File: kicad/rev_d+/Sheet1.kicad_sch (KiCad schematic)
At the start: 135 parts, among them J1 JUMPER, J11 JUMPER, J4 JUMPER, J7 JUMPER, Q1 14Mhz, X1 FDD34M, X2 IDE40M, X24 to extender/riser

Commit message: pentevo: rev D+: zx kbd
git-svn-id: svn://localhost/local-pentevo@1307 c6c76956-fad2-4150-a3a9-ea0a427205ba
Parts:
- removed R19: 390, R-CHIP, symbol eva-altium-import:Sheet1_0_RESCHIP
- removed VD3: LED, LED100, symbol eva-altium-import:Sheet1_0_mirrored_LED
- added VT10, VT9: BC857, Package_TO_SOT_SMD:SOT-23_Handsoldering, symbol Transistor_BJT:BC857
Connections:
- net GND: now also VT10.3 (C), VT9.3 (C)
- net ~{SDCS}: now also VT10.1 (B)
- net ILED: no longer names the net of X2.39 (~{DASP})
- net ILED: now also VT9.1 (B)
- new net ~{DISK_LED}: VT10.2 (E), VT9.2 (E)

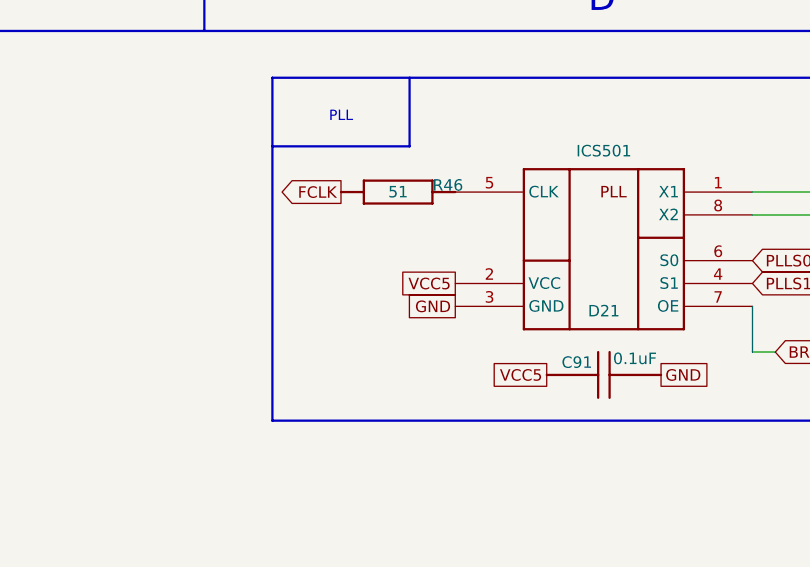
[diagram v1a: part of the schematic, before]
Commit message: pentevo: rev D+: return back shared UART between TTL and RS232, connect ROM high addrs to MCU
git-svn-id: svn://localhost/local-pentevo@1309 c6c76956-fad2-4150-a3a9-ea0a427205ba
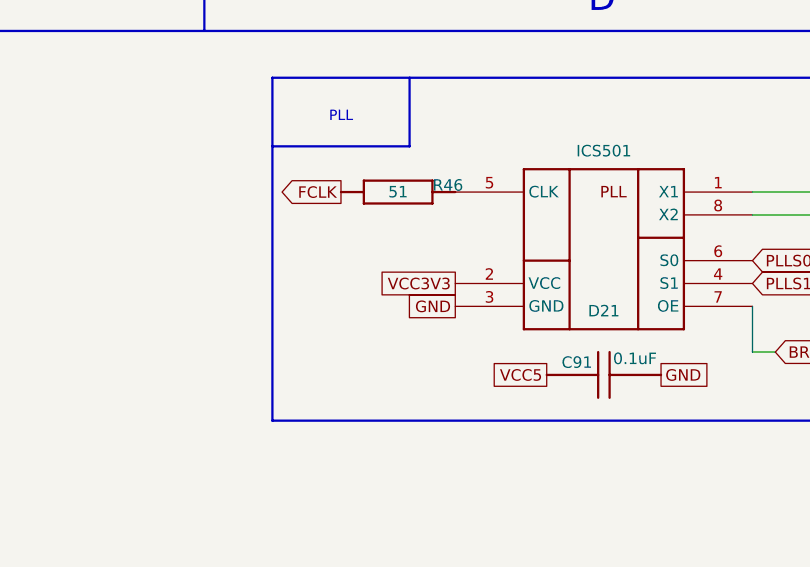
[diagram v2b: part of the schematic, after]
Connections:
- net VCC3V3: now also D21.2 (VCC)
- net VCC5: no longer D21.2 (VCC)
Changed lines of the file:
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@@
+		)
+	)
+	(global_label "VCC3V3"
+		(shape passive)
+		(at 307.34 55.88 180)
+		(fields_autoplaced yes)
+		(effects
+			(font
+				(size 1.27 1.27)
+			)
+			(justify right)
+		)
+		(property "Intersheetrefs" "${INTERSHEET_REFS}"
+			(at 298.3299 55.88 0)
+			(effects
+				(font
+					(size 1.27 1.27)
+				)
+				(justify right)
+				(hide yes)
+			)
 		)
 	)
@@
 			(effects
 				(font
-					(size 1.27 1.27)
-				)
-				(justify right)
-				(hide yes)
-			)
-		)
-	)
-	(global_label "VCC5"
-		(shape passive)
-		(at 307.34 55.88 180)
-		(fields_autoplaced yes)
-		(effects
-			(font
-				(size 1.27 1.27)
-			)
-			(justify right)
-		)
-		(property "Intersheetrefs" "${INTERSHEET_REFS}"
-			(at 300.628 55.88 0)
-			(effects
-				(font

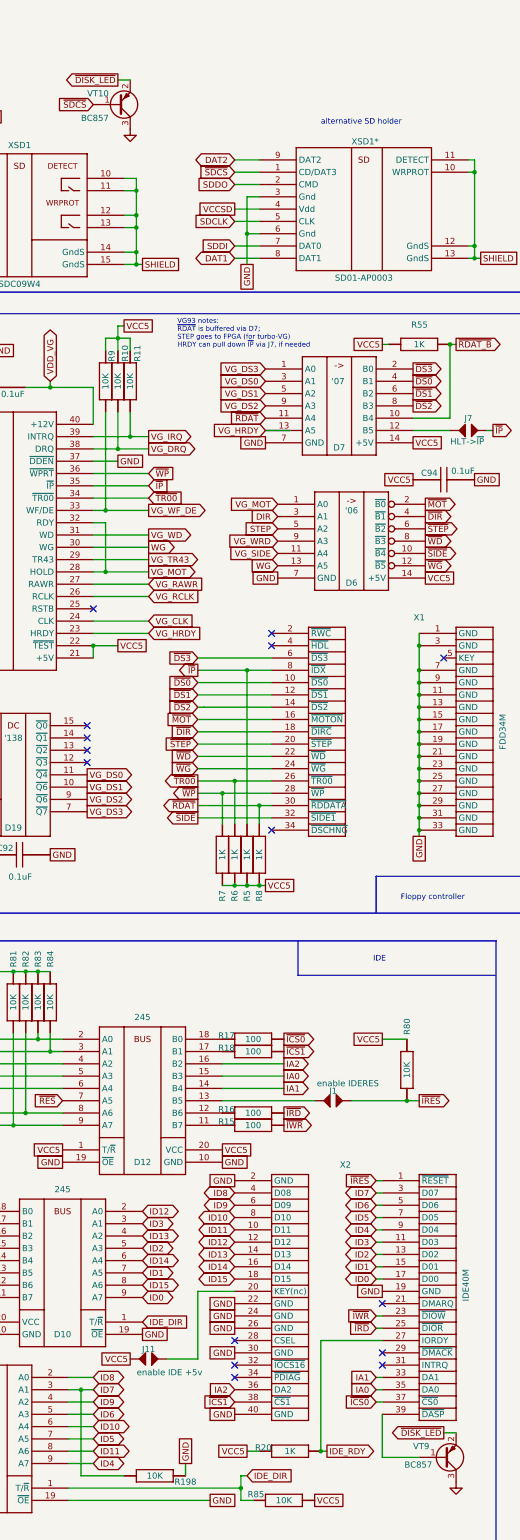
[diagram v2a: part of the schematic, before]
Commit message: pentevo: rev D+: fix I2C extender for segapads, remove 2N7002 from high ROM addresses, add I2C level convertor on 2N7002 (because of PCA9555 input levels)
git-svn-id: svn://localhost/local-pentevo@1311 c6c76956-fad2-4150-a3a9-ea0a427205ba
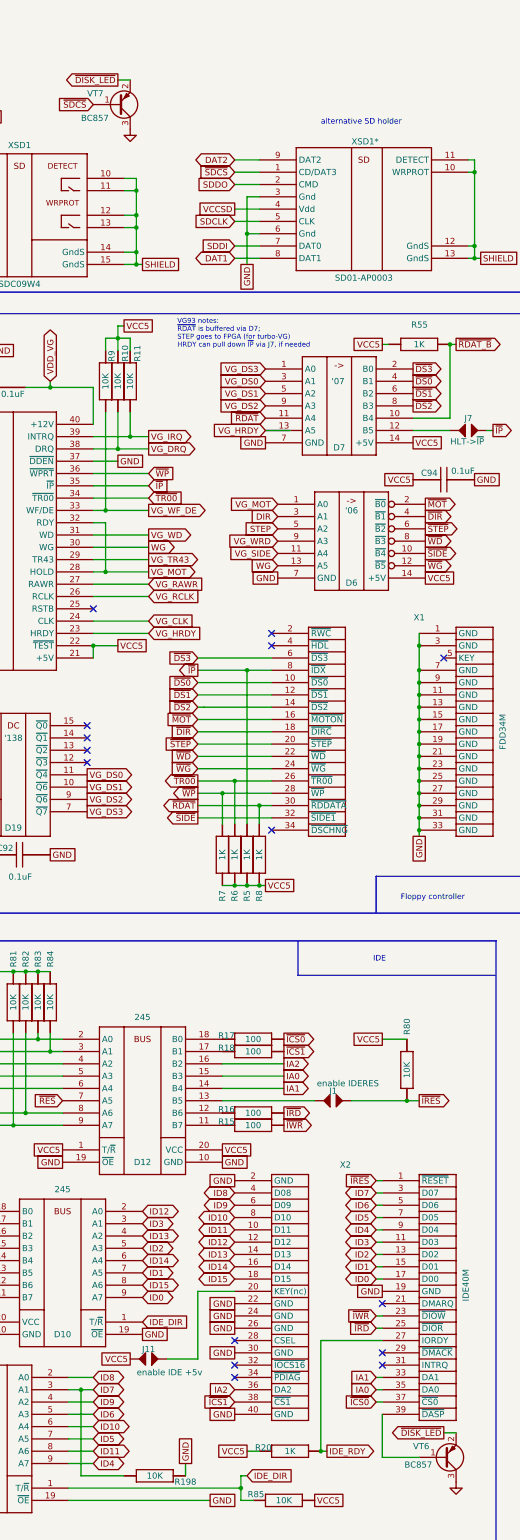
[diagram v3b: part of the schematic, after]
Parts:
- removed VT10, VT9: BC857, Package_TO_SOT_SMD:SOT-23_Handsoldering, symbol Transistor_BJT:BC857
- added VT6, VT7: BC857, Package_TO_SOT_SMD:SOT-23_Handsoldering, symbol Transistor_BJT:BC857
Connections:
- net GND: now also VT6.3 (C), VT7.3 (C)
- net ~{DISK_LED}: now also VT6.2 (E), VT7.2 (E)
- net ~{SDCS}: now also VT7.1 (B)
- net at X2.39 (~{DASP}): now also VT6.1 (B)
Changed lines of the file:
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@@
 	)
 	(symbol
-		(lib_id "Transistor_BJT:BC857")
-		(at 518.16 332.74 0)
-		(mirror x)
-		(unit 1)
-		(exclude_from_sim no)
-		(in_bom yes)
-		(on_board yes)
-		(dnp no)
-		(property "Reference" "VT9"
-			(at 511.81 330.454 0)
-			(effects
-				(font
-					(size 1.27 1.27)
-				)
-				(justify left)
-			)
-		)
-		(property "Value" "BC857"
-			(at 510.032 334.264 0)
-			(effects
-				(font
-					(size 1.27 1.27)
-				)
-				(justify left)
-			)
-		)
-		(property "Footprint" "Package_TO_SOT_SMD:SOT-23_Handsoldering"
-			(at 523.24 330.835 0)
-			(effects
-				(font
-					(size 1.27 1.27)
-					(italic yes)
-				)
-				(justify left)
-				(hide yes)
-			)
-		)
-		(property "Datasheet" "https://www.onsemi.com/pub/Collateral/BC860-D.pdf"
-			(at 518.16 332.74 0)
-			(effects
-				(font
-					(size 1.27 1.27)
-				)
-				(justify left)
-				(hide yes)
-			)
-		)
-		(property "Description" "0.1A Ic, 45V Vce, PNP Transistor, SOT-23"
-			(at 518.16 332.74 0)
-			(effects
-				(font
-					(size 1.27 1.27)
-				)
-				(hide yes)
-			)
-		)
-		(pin "1"
-		)
-		(pin "2"
-		)
-		(pin "3"
-		)
-		(instances
-			(project "eva"
-				(path "/ab605654-a730-497b-9e09-9b351f74b935/df95af23-acf0-4751-87c3-fbc71e0508c6"
-					(reference "VT9")
-					(unit 1)
-				)
-			)
-		)
-	)
-	(symbol
 		(lib_id "eva-altium-import:Sheet1_0_mirrored_04")
 		(at 147.32 59.69 0)
@@
 	)
 	(symbol
+		(lib_id "Transistor_BJT:BC857")
+		(at 450.85 53.34 0)
+		(mirror x)
+		(unit 1)
+		(exclude_from_sim no)
+		(in_bom yes)
+		(on_board yes)
+		(dnp no)
+		(property "Reference" "VT7"
+			(at 444.5 51.054 0)
+			(effects
+				(font
+					(size 1.27 1.27)
+				)
+				(justify left)
+			)
+		)
+		(property "Value" "BC857"
+			(at 443.23 56.134 0)
+			(effects
+				(font
+					(size 1.27 1.27)
+				)
+				(justify left)
+			)
+		)
+		(property "Footprint" "Package_TO_SOT_SMD:SOT-23_Handsoldering"
+			(at 455.93 51.435 0)
+			(effects
+				(font
+					(size 1.27 1.27)
+					(italic yes)
+				)
+				(justify left)
+				(hide yes)
+			)
+		)
+		(property "Datasheet" "https://www.onsemi.com/pub/Collateral/BC860-D.pdf"
+			(at 450.85 53.34 0)
+			(effects
+				(font
+					(size 1.27 1.27)
+				)
+				(justify left)
+				(hide yes)
+			)
+		)
+		(property "Description" "0.1A Ic, 45V Vce, PNP Transistor, SOT-23"
+			(at 450.85 53.34 0)
+			(effects
+				(font
+					(size 1.27 1.27)
+				)
+				(hide yes)
+			)
+		)
+		(pin "1"
+		)
+		(pin "2"
+		)
+		(pin "3"
+		)
+		(instances
+			(project "eva"
+				(path "/ab605654-a730-497b-9e09-9b351f74b935/df95af23-acf0-4751-87c3-fbc71e0508c6"
+					(reference "VT7")
+					(unit 1)
+				)
+			)
+		)
+	)
+	(symbol
 		(lib_id "eva-altium-import:Sheet1_0_CAPCHIP")
 		(at 419.1 111.76 0)
@@
 	)
 	(symbol
+		(lib_id "Transistor_BJT:BC857")
+		(at 518.16 332.74 0)
+		(mirror x)
+		(unit 1)
+		(exclude_from_sim no)
+		(in_bom yes)
+		(on_board yes)
+		(dnp no)
+		(property "Reference" "VT6"
+			(at 511.81 330.454 0)
+			(effects
+				(font
+					(size 1.27 1.27)
+				)
+				(justify left)
+			)
+		)
+		(property "Value" "BC857"
+			(at 510.032 334.264 0)
+			(effects
+				(font
+					(size 1.27 1.27)
+				)
+				(justify left)
+			)
+		)
+		(property "Footprint" "Package_TO_SOT_SMD:SOT-23_Handsoldering"
+			(at 523.24 330.835 0)
+			(effects
+				(font
+					(size 1.27 1.27)
+					(italic yes)
+				)
+				(justify left)
+				(hide yes)
+			)
+		)
+		(property "Datasheet" "https://www.onsemi.com/pub/Collateral/BC860-D.pdf"
+			(at 518.16 332.74 0)
+			(effects
+				(font
+					(size 1.27 1.27)
+				)
+				(justify left)
+				(hide yes)
+			)
+		)
+		(property "Description" "0.1A Ic, 45V Vce, PNP Transistor, SOT-23"
+			(at 518.16 332.74 0)
+			(effects
+				(font
+					(size 1.27 1.27)
+				)
+				(hide yes)
+			)
+		)
+		(pin "1"
+		)
+		(pin "2"
+		)
+		(pin "3"
+		)
+		(instances
+			(project "eva"
+				(path "/ab605654-a730-497b-9e09-9b351f74b935/df95af23-acf0-4751-87c3-fbc71e0508c6"
+					(reference "VT6")
+					(unit 1)
+				)
+			)
+		)
+	)
+	(symbol
 		(lib_id "eva-altium-import:Sheet1_0_ZXSLOT")
 		(at 73.66 299.72 0)
@@
 				)
 			)
-		)
-	)
-	(symbol
-		(lib_id "Transistor_BJT:BC857")
-		(at 450.85 53.34 0)
-		(mirror x)
-		(unit 1)
-		(exclude_from_sim no)
-		(in_bom yes)
-		(on_board yes)
-		(dnp no)
-		(property "Reference" "VT10"
-			(at 444.5 51.054 0)
-			(effects
-				(font
-					(size 1.27 1.27)
-				)
-				(justify left)
-			)
-		)
-		(property "Value" "BC857"
-			(at 443.23 56.134 0)
-			(effects
-				(font
-					(size 1.27 1.27)
-				)
-				(justify left)
-			)
-		)
-		(property "Footprint" "Package_TO_SOT_SMD:SOT-23_Handsoldering"
-			(at 455.93 51.435 0)
-			(effects
-				(font
-					(size 1.27 1.27)
-					(italic yes)
-				)
-				(justify left)
-				(hide yes)
-			)
-		)
-		(property "Datasheet" "https://www.onsemi.com/pub/Collateral/BC860-D.pdf"
-			(at 450.85 53.34 0)
-			(effects
-				(font
-					(size 1.27 1.27)
-				)
-				(justify left)
-				(hide yes)
-			)
-		)
-		(property "Description" "0.1A Ic, 45V Vce, PNP Transistor, SOT-23"
-			(at 450.85 53.34 0)
-			(effects
-				(font
-					(size 1.27 1.27)
-				)
-				(hide yes)
-			)
-		)
-		(pin "1"
-		)
-		(pin "2"
-		)
-		(pin "3"
-		)
-		(instances
-			(project "eva"
-				(path "/ab605654-a730-497b-9e09-9b351f74b935/df95af23-acf0-4751-87c3-fbc71e0508c6"
-					(reference "VT10")
-					(unit 1)
-				)
-			)

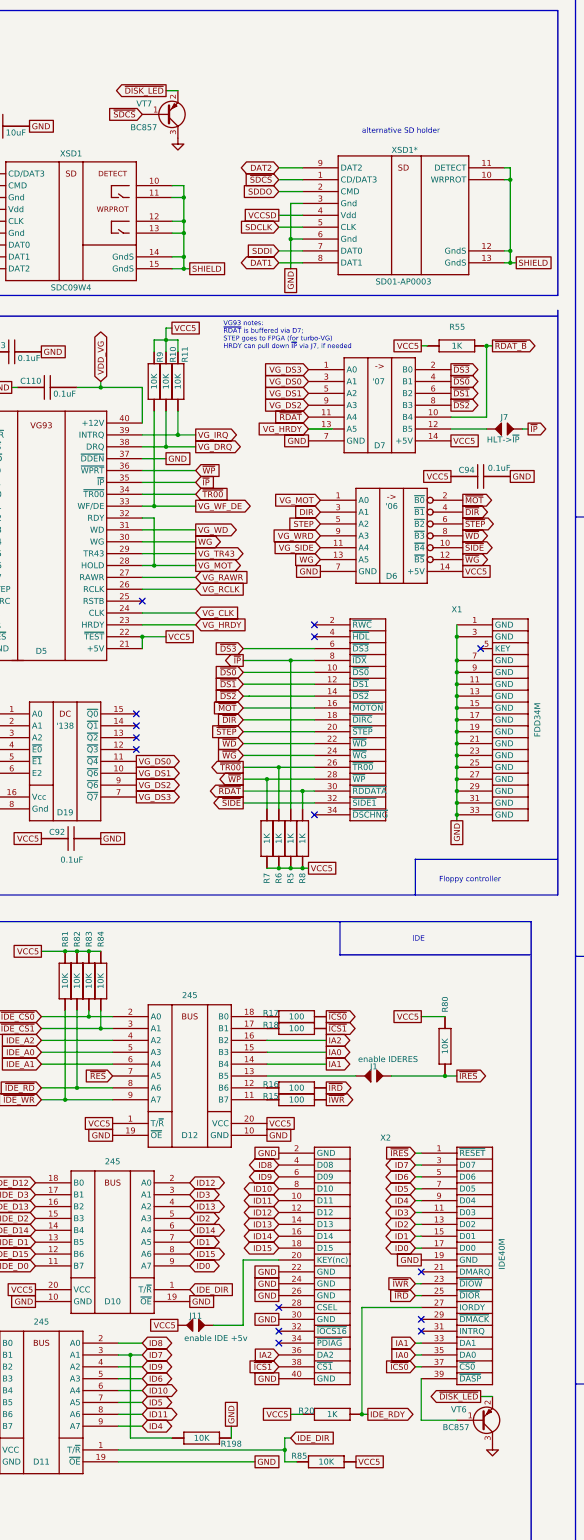
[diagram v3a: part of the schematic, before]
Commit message: pentevo: rev D+: add more usblc6, rearrange a bit
git-svn-id: svn://localhost/local-pentevo@1347 c6c76956-fad2-4150-a3a9-ea0a427205ba
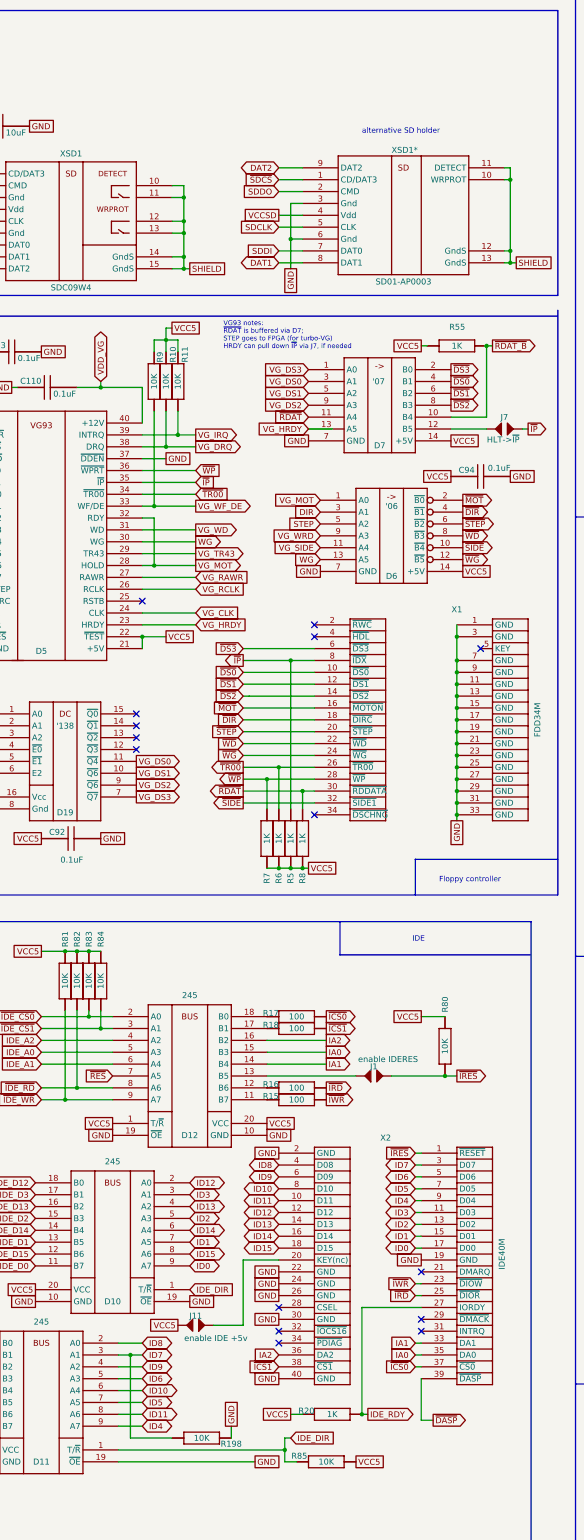
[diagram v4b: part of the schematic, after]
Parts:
- removed VT6, VT7: BC857, Package_TO_SOT_SMD:SOT-23_Handsoldering, symbol Transistor_BJT:BC857
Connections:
- net ~{DASP}: now reaches X2.39 (~{DASP})
